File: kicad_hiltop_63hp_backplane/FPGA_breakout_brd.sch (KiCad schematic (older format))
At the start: 31 parts, among them J11 SO-DIMM

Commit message: started simplifications to design
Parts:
- R5, R6, R84, R85, R86, R87, R88, R89, R90, R91: symbol device:R -> hiltop_backplane_brd-rescue:R-device
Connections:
- net GPIO_31: no longer R5.2
- net GPIO_32: no longer R6.2
- net GPIO_33: no longer R84.2
- net GPIO_34: no longer R85.2
- net GPIO_35: no longer R86.2
- net GPIO_36: no longer R87.2
- net GPIO_37: no longer R88.2
- net GPIO_38: no longer R89.2
- net GPIO_39: no longer R90.2
- net GPIO_40: no longer R91.2
- net GPIO_55: no longer R5.1
- net GPIO_56: no longer R6.1
- net GPIO_57: no longer R84.1
- net GPIO_58: no longer R85.1
- net GPIO_59: no longer R86.1
- net GPIO_60: no longer R87.1
- net GPIO_61: no longer R88.1
- net GPIO_62: no longer R89.1
- net GPIO_63: no longer R90.1
- net GPIO_64: no longer R91.1
- new net MBRD_GPIO10_IP: R91.1
- new net MBRD_GPIO10_OP: R91.2
- new net MBRD_GPIO1_IP: R5.1
- new net MBRD_GPIO1_OP: R5.2
- new net MBRD_GPIO2_IP: R6.1
- new net MBRD_GPIO2_OP: R6.2
- new net MBRD_GPIO3_IP: R84.1
- new net MBRD_GPIO3_OP: R84.2
- new net MBRD_GPIO4_IP: R85.1
- new net MBRD_GPIO4_OP: R85.2
- new net MBRD_GPIO5_IP: R86.1
- new net MBRD_GPIO5_OP: R86.2
- new net MBRD_GPIO6_IP: R87.1
- new net MBRD_GPIO6_OP: R87.2
- new net MBRD_GPIO7_IP: R88.1
- new net MBRD_GPIO7_OP: R88.2
- new net MBRD_GPIO8_IP: R89.1
- new net MBRD_GPIO8_OP: R89.2
- new net MBRD_GPIO9_IP: R90.1
- new net MBRD_GPIO9_OP: R90.2
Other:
- moved on the sheet: C22, C23, C24, C25, C26, C27, C28, C29, C30, C31, C32, C33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

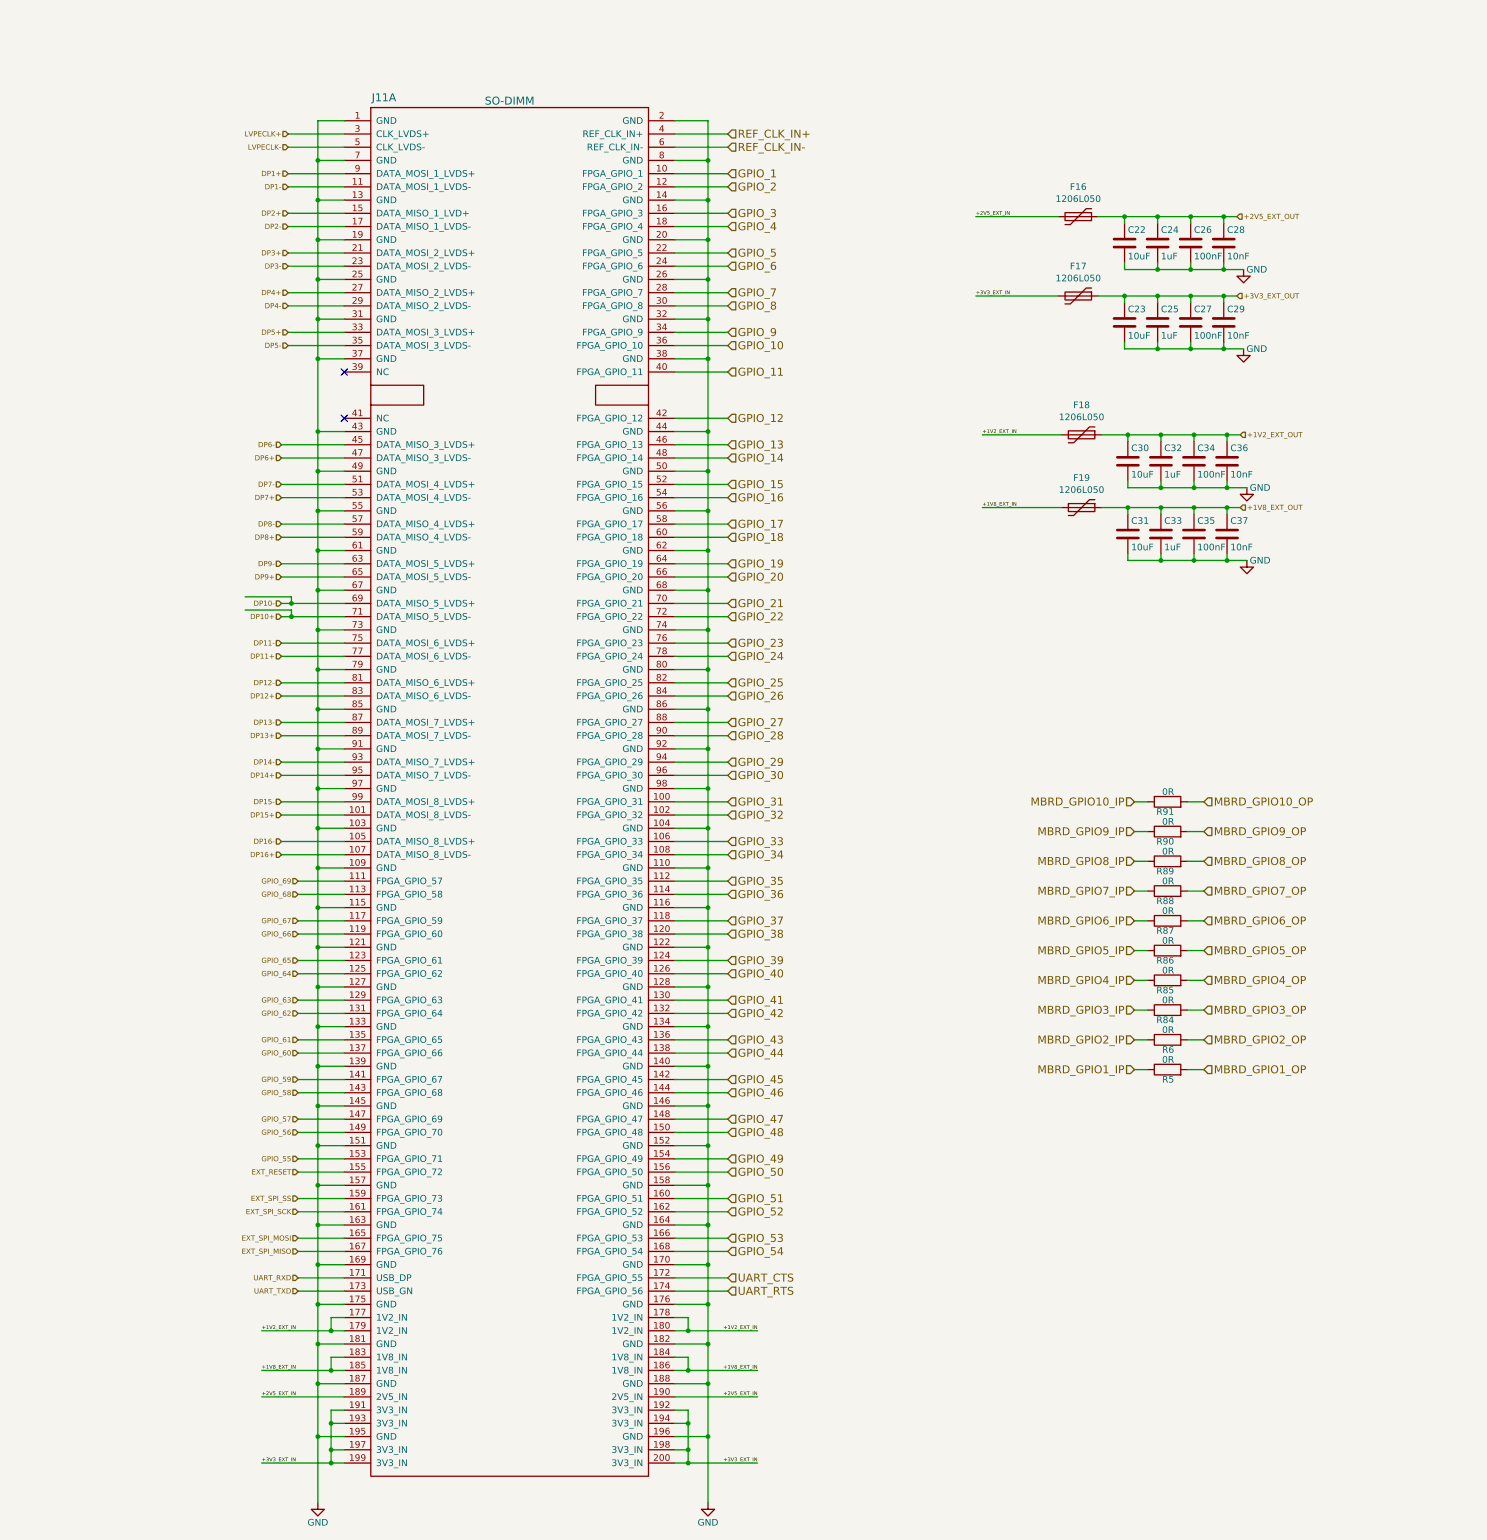
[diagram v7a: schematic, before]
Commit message: updated FPGA/SOC module pinouts
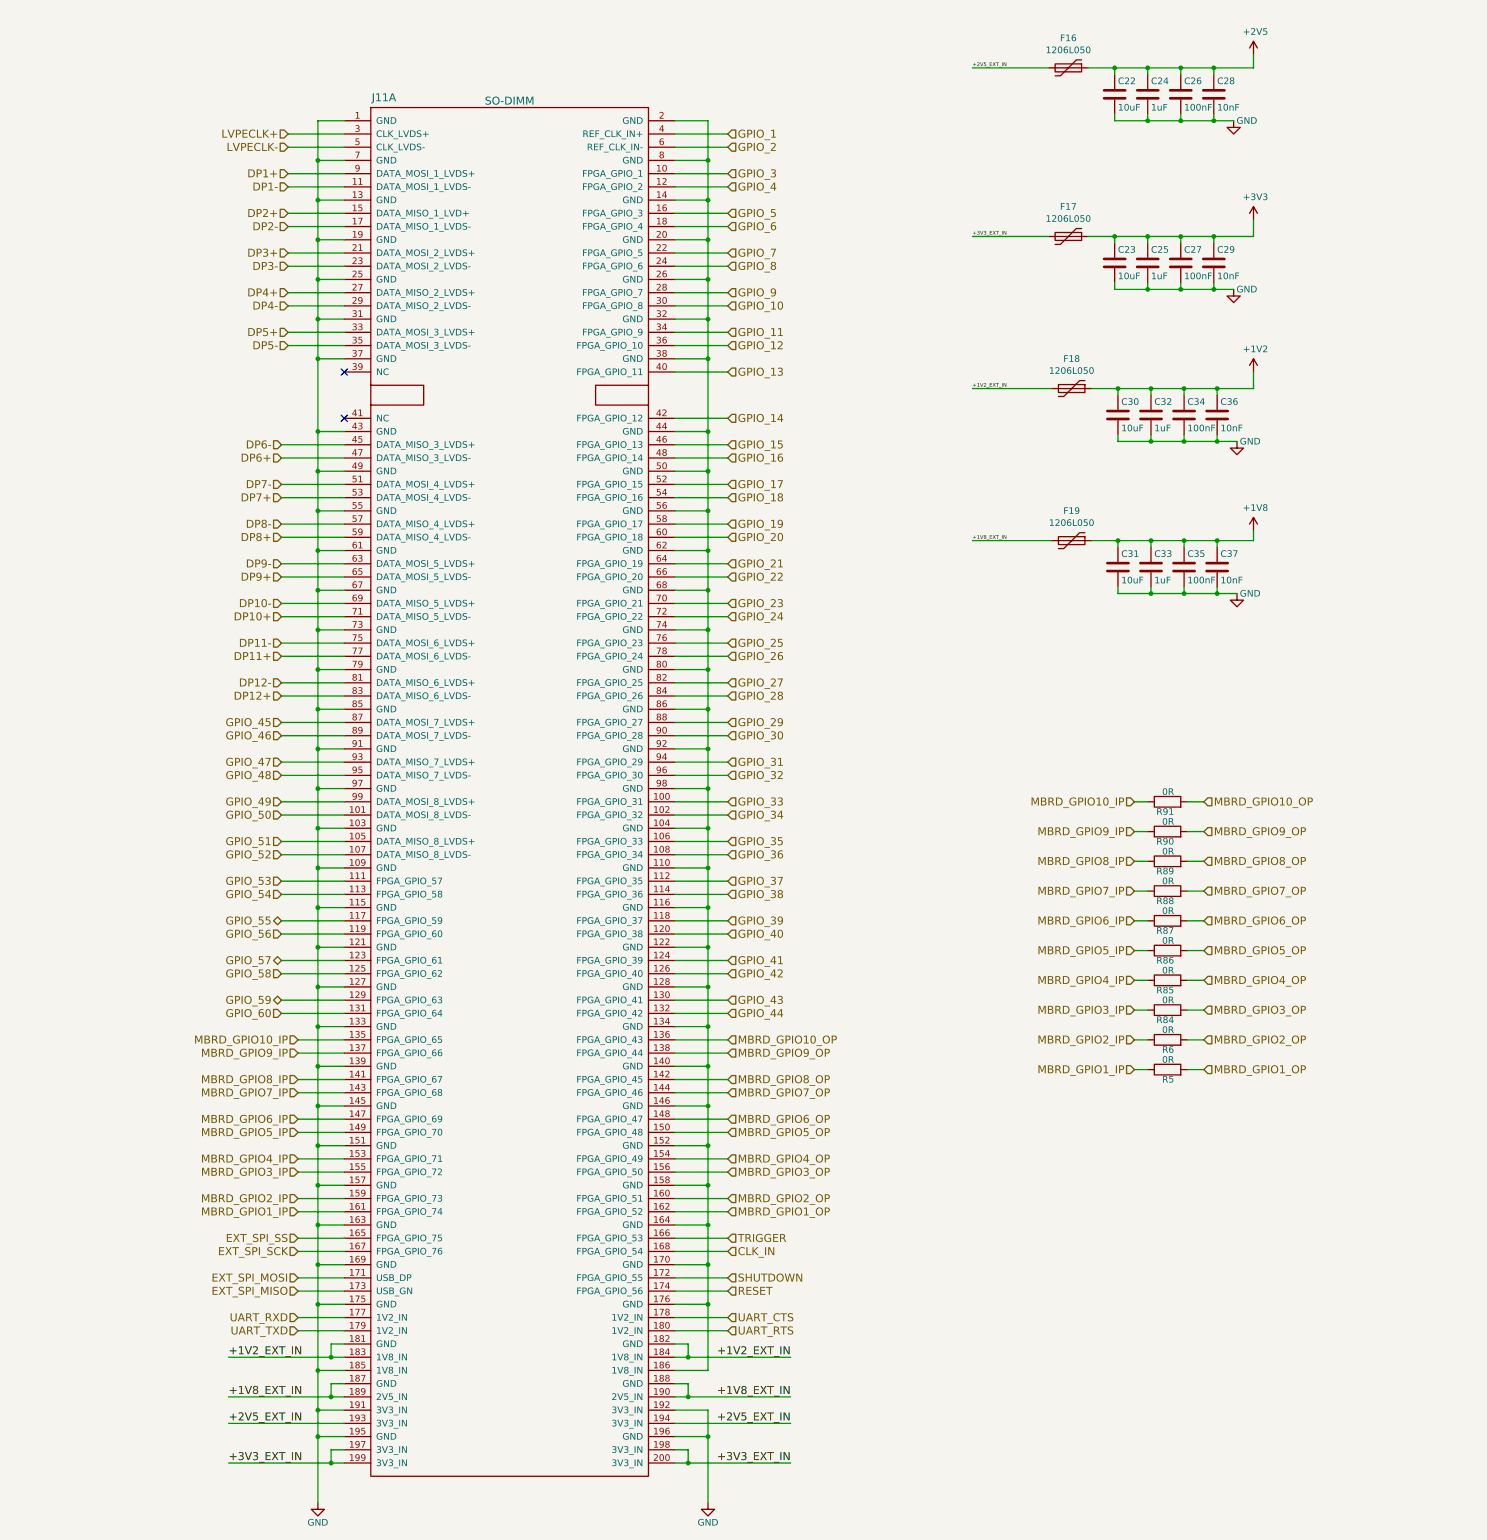
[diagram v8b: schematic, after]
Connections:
- net DP13+ is gone; now on net GPIO_46: J11.89 (DATA_MOSI_7_LVDS-)
- net DP13- is gone; now on net GPIO_45: J11.87 (DATA_MOSI_7_LVDS+)
- net DP14+ is gone; now on net GPIO_48: J11.95 (DATA_MISO_7_LVDS-)
- net DP14- is gone; now on net GPIO_47: J11.93 (DATA_MISO_7_LVDS+)
- net DP15+ is gone; now on net GPIO_50: J11.101 (DATA_MOSI_8_LVDS-)
- net DP15- is gone; now on net GPIO_49: J11.99 (DATA_MOSI_8_LVDS+)
- net DP16+ is gone; now on net GPIO_52: J11.107 (DATA_MISO_8_LVDS-)
- net DP16- is gone; now on net GPIO_51: J11.105 (DATA_MISO_8_LVDS+)
- net EXT_RESET is gone; now on net MBRD_GPIO3_IP: J11.155 (FPGA_GPIO_72)
- net GPIO_61 is gone; now on net MBRD_GPIO10_IP: J11.135 (FPGA_GPIO_65)
- net GPIO_62 is gone; now on net GPIO_60: J11.131 (FPGA_GPIO_64)
- net GPIO_63 is gone; now on net GPIO_59: J11.129 (FPGA_GPIO_63)
- net GPIO_64 is gone; now on net GPIO_58: J11.125 (FPGA_GPIO_62)
- net GPIO_65 is gone; now on net GPIO_57: J11.123 (FPGA_GPIO_61)
- net GPIO_66 is gone; now on net GPIO_56: J11.119 (FPGA_GPIO_60)
- net GPIO_67 is gone; now on net GPIO_55: J11.117 (FPGA_GPIO_59)
- net GPIO_68 is gone; now on net GPIO_54: J11.113 (FPGA_GPIO_58)
- net GPIO_69 is gone; now on net GPIO_53: J11.111 (FPGA_GPIO_57)
- net REF_CLK_IN+ is gone; now on net GPIO_1: J11.4 (REF_CLK_IN+)
- net REF_CLK_IN- is gone; now on net GPIO_2: J11.6 (REF_CLK_IN-)
- net +1V2_EXT_IN: now also J11.181 (GND), J11.182 (GND), J11.183 (1V8_IN), J11.184 (1V8_IN); no longer J11.177 (1V2_IN), J11.178 (1V2_IN), J11.179 (1V2_IN), J11.180 (1V2_IN)
- net +1V8_EXT_IN: now also J11.187 (GND), J11.188 (GND), J11.189 (2V5_IN), J11.190 (2V5_IN); no longer J11.183 (1V8_IN), J11.184 (1V8_IN), J11.185 (1V8_IN), J11.186 (1V8_IN)
- net +2V5_EXT_IN: now also J11.193 (3V3_IN), J11.194 (3V3_IN); no longer J11.189 (2V5_IN), J11.190 (2V5_IN)
- net +3V3_EXT_IN: no longer J11.191 (3V3_IN), J11.192 (3V3_IN), J11.193 (3V3_IN), J11.194 (3V3_IN)
- net EXT_SPI_MISO: now also J11.173 (USB_GN); no longer J11.167 (FPGA_GPIO_76)
- net EXT_SPI_MOSI: now also J11.171 (USB_DP); no longer J11.165 (FPGA_GPIO_75)
- net EXT_SPI_SCK: now also J11.167 (FPGA_GPIO_76); no longer J11.161 (FPGA_GPIO_74)
- net EXT_SPI_SS: now also J11.165 (FPGA_GPIO_75); no longer J11.159 (FPGA_GPIO_73)
- net GND: now also J11.185 (1V8_IN), J11.191 (3V3_IN), J11.192 (3V3_IN); no longer J11.104 (GND), J11.110 (GND), J11.116 (GND), J11.122 (GND), J11.128 (GND), J11.134 (GND), J11.14 (GND), J11.140 (GND), J11.146 (GND), J11.152 (GND), J11.158 (GND), J11.164 (GND), J11.170 (GND), J11.176 (GND), J11.181 (GND), J11.182 (GND), J11.187 (GND), J11.188 (GND), J11.2 (GND), J11.20 (GND), J11.26 (GND), J11.32 (GND), J11.38 (GND), J11.44 (GND), J11.50 (GND), J11.56 (GND), J11.62 (GND), J11.68 (GND), J11.74 (GND), J11.8 (GND), J11.80 (GND), J11.86 (GND), J11.92 (GND), J11.98 (GND)
- net GPIO_1: no longer J11.10 (FPGA_GPIO_1)
- net GPIO_10: now also J11.30 (FPGA_GPIO_8); no longer J11.36 (FPGA_GPIO_10)
- net GPIO_11: now also J11.34 (FPGA_GPIO_9); no longer J11.40 (FPGA_GPIO_11)
- net GPIO_12: now also J11.36 (FPGA_GPIO_10); no longer J11.42 (FPGA_GPIO_12)
- net GPIO_13: now also J11.40 (FPGA_GPIO_11); no longer J11.46 (FPGA_GPIO_13)
- net GPIO_14: now also J11.42 (FPGA_GPIO_12); no longer J11.48 (FPGA_GPIO_14)
- net GPIO_15: now also J11.46 (FPGA_GPIO_13); no longer J11.52 (FPGA_GPIO_15)
- net GPIO_16: now also J11.48 (FPGA_GPIO_14); no longer J11.54 (FPGA_GPIO_16)
- net GPIO_17: now also J11.52 (FPGA_GPIO_15); no longer J11.58 (FPGA_GPIO_17)
- net GPIO_18: now also J11.54 (FPGA_GPIO_16); no longer J11.60 (FPGA_GPIO_18)
- net GPIO_19: now also J11.58 (FPGA_GPIO_17); no longer J11.64 (FPGA_GPIO_19)
- net GPIO_2: no longer J11.12 (FPGA_GPIO_2)
- net GPIO_20: now also J11.60 (FPGA_GPIO_18); no longer J11.66 (FPGA_GPIO_20)
- net GPIO_21: now also J11.64 (FPGA_GPIO_19); no longer J11.70 (FPGA_GPIO_21)
- net GPIO_22: now also J11.66 (FPGA_GPIO_20); no longer J11.72 (FPGA_GPIO_22)
- net GPIO_23: now also J11.70 (FPGA_GPIO_21); no longer J11.76 (FPGA_GPIO_23)
- net GPIO_24: now also J11.72 (FPGA_GPIO_22); no longer J11.78 (FPGA_GPIO_24)
- net GPIO_25: now also J11.76 (FPGA_GPIO_23); no longer J11.82 (FPGA_GPIO_25)
- net GPIO_26: now also J11.78 (FPGA_GPIO_24); no longer J11.84 (FPGA_GPIO_26)
- net GPIO_27: now also J11.82 (FPGA_GPIO_25); no longer J11.88 (FPGA_GPIO_27)
- net GPIO_28: now also J11.84 (FPGA_GPIO_26); no longer J11.90 (FPGA_GPIO_28)
- net GPIO_29: now also J11.88 (FPGA_GPIO_27); no longer J11.94 (FPGA_GPIO_29)
- net GPIO_3: now also J11.10 (FPGA_GPIO_1); no longer J11.16 (FPGA_GPIO_3)
- net GPIO_30: now also J11.90 (FPGA_GPIO_28); no longer J11.96 (FPGA_GPIO_30)
- net GPIO_31: now also J11.94 (FPGA_GPIO_29); no longer J11.100 (FPGA_GPIO_31)
- net GPIO_32: now also J11.96 (FPGA_GPIO_30); no longer J11.102 (FPGA_GPIO_32)
- net GPIO_33: now also J11.100 (FPGA_GPIO_31); no longer J11.106 (FPGA_GPIO_33)
- net GPIO_34: now also J11.102 (FPGA_GPIO_32); no longer J11.108 (FPGA_GPIO_34)
- net GPIO_35: now also J11.106 (FPGA_GPIO_33); no longer J11.112 (FPGA_GPIO_35)
- net GPIO_36: now also J11.108 (FPGA_GPIO_34); no longer J11.114 (FPGA_GPIO_36)
- net GPIO_37: now also J11.112 (FPGA_GPIO_35); no longer J11.118 (FPGA_GPIO_37)
- net GPIO_38: now also J11.114 (FPGA_GPIO_36); no longer J11.120 (FPGA_GPIO_38)
- net GPIO_39: now also J11.118 (FPGA_GPIO_37); no longer J11.124 (FPGA_GPIO_39)
- net GPIO_4: now also J11.12 (FPGA_GPIO_2); no longer J11.18 (FPGA_GPIO_4)
- net GPIO_40: now also J11.120 (FPGA_GPIO_38); no longer J11.126 (FPGA_GPIO_40)
- net GPIO_41: now also J11.124 (FPGA_GPIO_39); no longer J11.130 (FPGA_GPIO_41)
- net GPIO_42: now also J11.126 (FPGA_GPIO_40); no longer J11.132 (FPGA_GPIO_42)
- net GPIO_43: now also J11.130 (FPGA_GPIO_41); no longer J11.136 (FPGA_GPIO_43)
- net GPIO_44: now also J11.132 (FPGA_GPIO_42); no longer J11.138 (FPGA_GPIO_44)
- net GPIO_45: no longer J11.142 (FPGA_GPIO_45)
- net GPIO_46: no longer J11.144 (FPGA_GPIO_46)
- net GPIO_47: no longer J11.148 (FPGA_GPIO_47)
- net GPIO_48: no longer J11.150 (FPGA_GPIO_48)
- net GPIO_49: no longer J11.154 (FPGA_GPIO_49)
- net GPIO_5: now also J11.16 (FPGA_GPIO_3); no longer J11.22 (FPGA_GPIO_5)
- net GPIO_50: no longer J11.156 (FPGA_GPIO_50)
- net GPIO_51: no longer J11.160 (FPGA_GPIO_51)
- net GPIO_52: no longer J11.162 (FPGA_GPIO_52)
- net GPIO_53: no longer J11.166 (FPGA_GPIO_53)
- net GPIO_54: no longer J11.168 (FPGA_GPIO_54)
- net GPIO_55: no longer J11.153 (FPGA_GPIO_71)
- net GPIO_56: no longer J11.149 (FPGA_GPIO_70)
- net GPIO_57: no longer J11.147 (FPGA_GPIO_69)
- net GPIO_58: no longer J11.143 (FPGA_GPIO_68)
- net GPIO_59: no longer J11.141 (FPGA_GPIO_67)
- net GPIO_6: now also J11.18 (FPGA_GPIO_4); no longer J11.24 (FPGA_GPIO_6)
- net GPIO_60: no longer J11.137 (FPGA_GPIO_66)
- net GPIO_7: now also J11.22 (FPGA_GPIO_5); no longer J11.28 (FPGA_GPIO_7)
- net GPIO_8: now also J11.24 (FPGA_GPIO_6); no longer J11.30 (FPGA_GPIO_8)
- net GPIO_9: now also J11.28 (FPGA_GPIO_7); no longer J11.34 (FPGA_GPIO_9)
- net MBRD_GPIO10_OP: now also J11.136 (FPGA_GPIO_43)
- net MBRD_GPIO1_IP: now also J11.161 (FPGA_GPIO_74)
- net MBRD_GPIO1_OP: now also J11.162 (FPGA_GPIO_52)
- net MBRD_GPIO2_IP: now also J11.159 (FPGA_GPIO_73)
- net MBRD_GPIO2_OP: now also J11.160 (FPGA_GPIO_51)
- net MBRD_GPIO3_OP: now also J11.156 (FPGA_GPIO_50)
- net MBRD_GPIO4_IP: now also J11.153 (FPGA_GPIO_71)
- net MBRD_GPIO4_OP: now also J11.154 (FPGA_GPIO_49)
- net MBRD_GPIO5_IP: now also J11.149 (FPGA_GPIO_70)
- net MBRD_GPIO5_OP: now also J11.150 (FPGA_GPIO_48)
- net MBRD_GPIO6_IP: now also J11.147 (FPGA_GPIO_69)
- net MBRD_GPIO6_OP: now also J11.148 (FPGA_GPIO_47)
- net MBRD_GPIO7_IP: now also J11.143 (FPGA_GPIO_68)
- net MBRD_GPIO7_OP: now also J11.144 (FPGA_GPIO_46)
- net MBRD_GPIO8_IP: now also J11.141 (FPGA_GPIO_67)
- net MBRD_GPIO8_OP: now also J11.142 (FPGA_GPIO_45)
- net MBRD_GPIO9_IP: now also J11.137 (FPGA_GPIO_66)
- net MBRD_GPIO9_OP: now also J11.138 (FPGA_GPIO_44)
- net UART_CTS: now also J11.178 (1V2_IN); no longer J11.172 (FPGA_GPIO_55)
- net UART_RTS: now also J11.180 (1V2_IN); no longer J11.174 (FPGA_GPIO_56)
- net UART_RXD: now also J11.177 (1V2_IN); no longer J11.171 (USB_DP)
- net UART_TXD: now also J11.179 (1V2_IN); no longer J11.173 (USB_GN)
- net +1V2_EXT_OUT renamed +1V2
- net +1V8_EXT_OUT renamed +1V8
- net +2V5_EXT_OUT renamed +2V5
- net +3V3_EXT_OUT renamed +3V3
- new net: J11.104 (GND), J11.110 (GND), J11.116 (GND), J11.122 (GND), J11.128 (GND), J11.134 (GND), J11.14 (GND), J11.140 (GND), J11.146 (GND), J11.152 (GND), J11.158 (GND), J11.164 (GND), J11.170 (GND), J11.176 (GND), J11.186 (1V8_IN), J11.2 (GND), J11.20 (GND), J11.26 (GND), J11.32 (GND), J11.38 (GND), J11.44 (GND), J11.50 (GND), J11.56 (GND), J11.62 (GND), J11.68 (GND), J11.74 (GND), J11.8 (GND), J11.80 (GND), J11.86 (GND), J11.92 (GND), J11.98 (GND)
- new net CLK_IN: J11.168 (FPGA_GPIO_54)
- new net RESET: J11.174 (FPGA_GPIO_56)
- new net SHUTDOWN: J11.172 (FPGA_GPIO_55)
- new net TRIGGER: J11.166 (FPGA_GPIO_53)
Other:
- moved on the sheet: C22, C23, C24, C25, C26, C27, C28, C29, C30, C31, C32, C33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
